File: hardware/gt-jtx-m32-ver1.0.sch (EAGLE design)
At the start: 11 parts, among them IC1 MEGA32-P

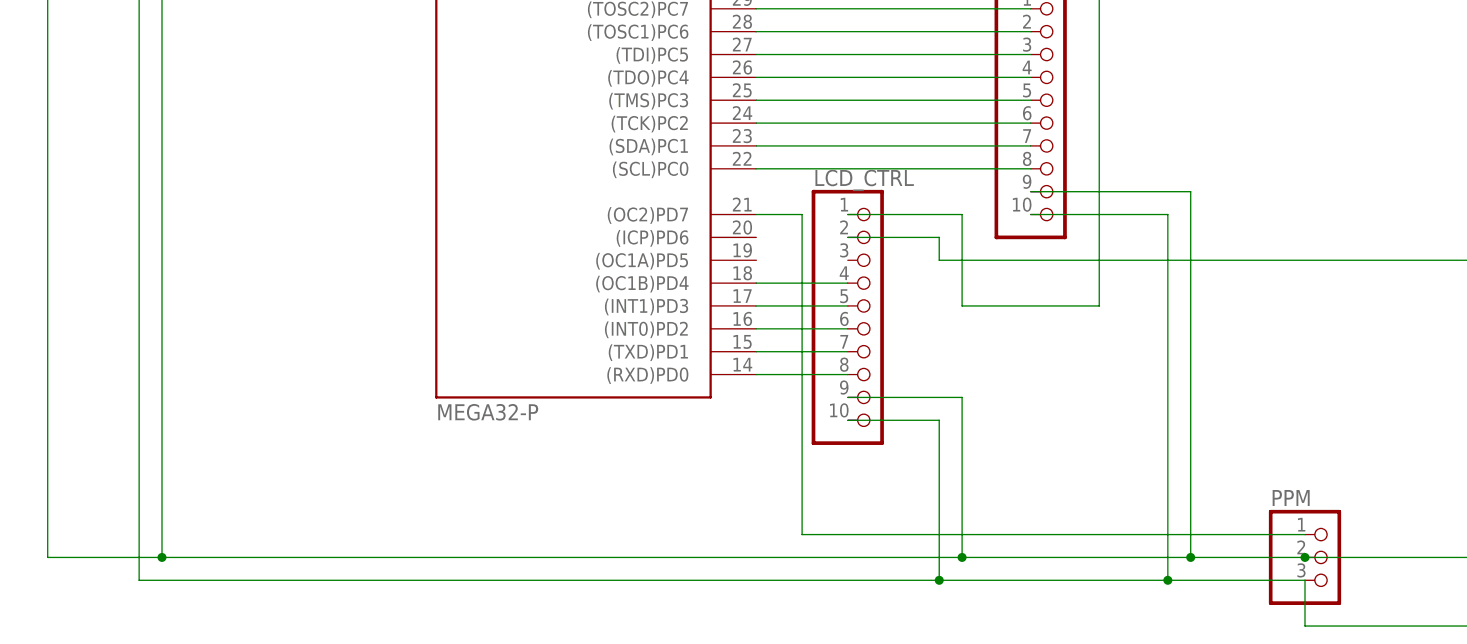
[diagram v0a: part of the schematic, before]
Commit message: added speaker and switch ports changed ppm pin to PD5
git-svn-id: https://gt-jtx.googlecode.com/svn/trunk@69 79910f2a-facc-22ab-b1ea-80da55196309
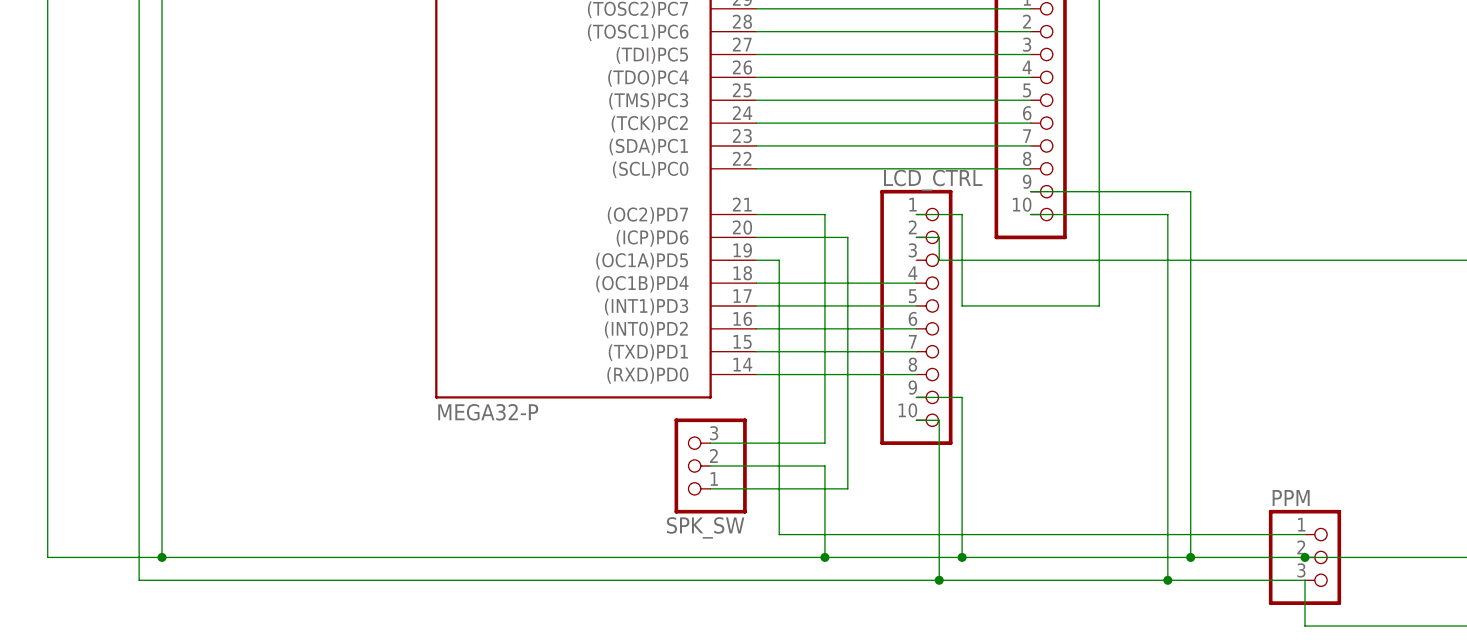
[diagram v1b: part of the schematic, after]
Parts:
- added SPK_SW: (no value), pinhead:PINHD-1X3
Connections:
- removed net GND: ANALOG.1, IC1.GND, IC1.GND@1, LCD_CTRL.9, LCD_DATA.9, LED.C, PPM.2, PWR.2, TRIMS.1, VR1.E
- new net N$5: IC1.(ICP)PD6, SPK_SW.1
- new net N$6: IC1.(OC2)PD7, SPK_SW.3
- new net SPK_SW: ANALOG.1, IC1.GND, IC1.GND@1, LCD_CTRL.9, LCD_DATA.9, LED.C, PPM.2, PWR.2, SPK_SW.2, TRIMS.1, VR1.E
- net N$15: now also IC1.(OC1A)PD5; no longer IC1.(OC2)PD7
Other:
- moved on the sheet: LCD_CTRL
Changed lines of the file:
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@@
 <part name="LCD_CTRL" library="pinhead" deviceset="PINHD-1X10" device=""/>
 <part name="LCD_DATA" library="pinhead" deviceset="PINHD-1X10" device=""/>
+<part name="SPK_SW" library="pinhead" deviceset="PINHD-1X3" device=""/>
 </parts>
 <sheets>
@@
 <instance part="ISP" gate="A" x="162.56" y="144.78"/>
 <instance part="IC1" gate="G$1" x="93.98" y="124.46"/>
-<instance part="LCD_CTRL" gate="A" x="127" y="88.9"/>
+<instance part="LCD_CTRL" gate="A" x="134.62" y="88.9"/>
 <instance part="LCD_DATA" gate="A" x="147.32" y="111.76"/>
+<instance part="SPK_SW" gate="A" x="106.68" y="71.12" rot="R180"/>
 </instances>
 <busses>
@@
 <pinref part="LCD_CTRL" gate="A" pin="10"/>
 <wire x1="205.74" y1="106.68" x2="205.74" y2="142.24" width="0.1524" layer="91"/>
-<wire x1="124.46" y1="76.2" x2="134.62" y2="76.2" width="0.1524" layer="91"/>
+<wire x1="132.08" y1="76.2" x2="134.62" y2="76.2" width="0.1524" layer="91"/>
 <wire x1="134.62" y1="76.2" x2="134.62" y2="58.42" width="0.1524" layer="91"/>
 <junction x="134.62" y="58.42"/>
@@
 </segment>
 </net>
-<net name="GND" class="0">
+<net name="SPK_SW" class="0">
 <segment>
 <wire x1="73.66" y1="144.78" x2="48.26" y2="144.78" width="0.1524" layer="91"/>
@@
 <wire x1="35.56" y1="154.94" x2="35.56" y2="60.96" width="0.1524" layer="91"/>
 <wire x1="35.56" y1="60.96" x2="48.26" y2="60.96" width="0.1524" layer="91"/>
-<wire x1="48.26" y1="60.96" x2="137.16" y2="60.96" width="0.1524" layer="91"/>
+<wire x1="48.26" y1="60.96" x2="121.92" y2="60.96" width="0.1524" layer="91"/>
+<wire x1="121.92" y1="60.96" x2="137.16" y2="60.96" width="0.1524" layer="91"/>
 <wire x1="137.16" y1="60.96" x2="162.56" y2="60.96" width="0.1524" layer="91"/>
 <wire x1="162.56" y1="60.96" x2="175.26" y2="60.96" width="0.1524" layer="91"/>
@@
 <pinref part="LCD_CTRL" gate="A" pin="9"/>
 <wire x1="220.98" y1="106.68" x2="220.98" y2="147.32" width="0.1524" layer="91"/>
-<wire x1="124.46" y1="78.74" x2="137.16" y2="78.74" width="0.1524" layer="91"/>
+<wire x1="132.08" y1="78.74" x2="137.16" y2="78.74" width="0.1524" layer="91"/>
 <wire x1="137.16" y1="78.74" x2="137.16" y2="60.96" width="0.1524" layer="91"/>
 <junction x="137.16" y="60.96"/>
@@
 <wire x1="162.56" y1="101.6" x2="162.56" y2="60.96" width="0.1524" layer="91"/>
 <junction x="162.56" y="60.96"/>
+<pinref part="SPK_SW" gate="A" pin="2"/>
+<wire x1="109.22" y1="71.12" x2="121.92" y2="71.12" width="0.1524" layer="91"/>
+<wire x1="121.92" y1="71.12" x2="121.92" y2="60.96" width="0.1524" layer="91"/>
+<junction x="121.92" y="60.96"/>
 </segment>
 </net>
@@
 <junction x="73.66" y="167.64"/>
 <pinref part="LCD_CTRL" gate="A" pin="1"/>
-<wire x1="124.46" y1="99.06" x2="137.16" y2="99.06" width="0.1524" layer="91"/>
+<wire x1="132.08" y1="99.06" x2="137.16" y2="99.06" width="0.1524" layer="91"/>
 <wire x1="137.16" y1="99.06" x2="137.16" y2="88.9" width="0.1524" layer="91"/>
 <wire x1="137.16" y1="88.9" x2="152.4" y2="88.9" width="0.1524" layer="91"/>
@@
 <pinref part="IC1" gate="G$1" pin="(RXD)PD0"/>
 <pinref part="LCD_CTRL" gate="A" pin="8"/>
-<wire x1="114.3" y1="81.28" x2="124.46" y2="81.28" width="0.1524" layer="91"/>
+<wire x1="114.3" y1="81.28" x2="132.08" y2="81.28" width="0.1524" layer="91"/>
 </segment>
 </net>
@@
 <pinref part="IC1" gate="G$1" pin="(TXD)PD1"/>
 <pinref part="LCD_CTRL" gate="A" pin="7"/>
-<wire x1="114.3" y1="83.82" x2="124.46" y2="83.82" width="0.1524" layer="91"/>
+<wire x1="114.3" y1="83.82" x2="132.08" y2="83.82" width="0.1524" layer="91"/>
 </segment>
 </net>
@@
 <pinref part="IC1" gate="G$1" pin="(INT0)PD2"/>
 <pinref part="LCD_CTRL" gate="A" pin="6"/>
-<wire x1="114.3" y1="86.36" x2="124.46" y2="86.36" width="0.1524" layer="91"/>
+<wire x1="114.3" y1="86.36" x2="132.08" y2="86.36" width="0.1524" layer="91"/>
 </segment>
 </net>
@@
 <pinref part="IC1" gate="G$1" pin="(INT1)PD3"/>
 <pinref part="LCD_CTRL" gate="A" pin="5"/>
-<wire x1="114.3" y1="88.9" x2="124.46" y2="88.9" width="0.1524" layer="91"/>
+<wire x1="114.3" y1="88.9" x2="132.08" y2="88.9" width="0.1524" layer="91"/>
 </segment>
 </net>
@@
 <pinref part="IC1" gate="G$1" pin="(OC1B)PD4"/>
 <pinref part="LCD_CTRL" gate="A" pin="4"/>
-<wire x1="114.3" y1="91.44" x2="124.46" y2="91.44" width="0.1524" layer="91"/>
+<wire x1="114.3" y1="91.44" x2="132.08" y2="91.44" width="0.1524" layer="91"/>
 </segment>
 </net>
@@
 <segment>
 <pinref part="LCD_CTRL" gate="A" pin="2"/>
-<wire x1="124.46" y1="96.52" x2="134.62" y2="96.52" width="0.1524" layer="91"/>
+<wire x1="132.08" y1="96.52" x2="134.62" y2="96.52" width="0.1524" layer="91"/>
 <wire x1="134.62" y1="96.52" x2="134.62" y2="93.98" width="0.1524" layer="91"/>
 <wire x1="134.62" y1="93.98" x2="213.36" y2="93.98" width="0.1524" layer="91"/>
@@
 <net name="N$15" class="0">
 <segment>
+<pinref part="PPM" gate="A" pin="1"/>
+<wire x1="116.84" y1="93.98" x2="116.84" y2="63.5" width="0.1524" layer="91"/>
+<wire x1="116.84" y1="63.5" x2="175.26" y2="63.5" width="0.1524" layer="91"/>
+<pinref part="IC1" gate="G$1" pin="(OC1A)PD5"/>
+<wire x1="114.3" y1="93.98" x2="116.84" y2="93.98" width="0.1524" layer="91"/>
+</segment>
+</net>
+<net name="N$5" class="0">
+<segment>
+<pinref part="SPK_SW" gate="A" pin="1"/>
+<wire x1="109.22" y1="68.58" x2="124.46" y2="68.58" width="0.1524" layer="91"/>
+<wire x1="124.46" y1="68.58" x2="124.46" y2="96.52" width="0.1524" layer="91"/>
+<pinref part="IC1" gate="G$1" pin="(ICP)PD6"/>
+<wire x1="124.46" y1="96.52" x2="114.3" y2="96.52" width="0.1524" layer="91"/>
+</segment>
+</net>
+<net name="N$6" class="0">
+<segment>
+<pinref part="SPK_SW" gate="A" pin="3"/>
+<wire x1="109.22" y1="73.66" x2="121.92" y2="73.66" width="0.1524" layer="91"/>
+<wire x1="121.92" y1="73.66" x2="121.92" y2="99.06" width="0.1524" layer="91"/>
 <pinref part="IC1" gate="G$1" pin="(OC2)PD7"/>
-<wire x1="114.3" y1="99.06" x2="119.38" y2="99.06" width="0.1524" layer="91"/>
-<wire x1="119.38" y1="99.06" x2="119.38" y2="63.5" width="0.1524" layer="91"/>
-<pinref part="PPM" gate="A" pin="1"/>
-<wire x1="119.38" y1="63.5" x2="175.26" y2="63.5" width="0.1524" layer="91"/>
-</segment>
-</net>
+<wire x1="121.92" y1="99.06" x2="114.3" y2="99.06" width="0.1524" layer="91"/>
+</segment>
+</net>

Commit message: fixed some of the hardware design
git-svn-id: https://gt-jtx.googlecode.com/svn/trunk@70 79910f2a-facc-22ab-b1ea-80da55196309
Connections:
- removed net N$33: IC1.(MOSI)PB5, ISP.6, TRIMS.5
- removed net N$34: IC1.(MISO)PB6, ISP.5, TRIMS.4
- removed net RST: IC1.RESET, ISP.1, LCD_CTRL.1, R2.2
- removed net SPK_SW: ANALOG.1, IC1.GND, IC1.GND@1, LCD_CTRL.9, LCD_DATA.9, LED.C, PPM.2, PWR.2, SPK_SW.2, TRIMS.1, VR1.E
- new net GND: ANALOG.1, IC1.GND, IC1.GND@1, ISP.1, LCD_CTRL.2, LCD_DATA.9, LED.C, PPM.2, PWR.2, SPK_SW.2, TRIMS.2, VR1.E
- new net N$12: IC1.(MOSI)PB5, ISP.6
- new net N$13: IC1.(MISO)PB6, ISP.2
- new net N$14: IC1.(SCK)PB7, ISP.3
- new net N$9: IC1.RESET, ISP.4, LCD_CTRL.10, R2.2
- net +5V: now also ISP.5, LCD_CTRL.1, TRIMS.1; no longer ISP.3, LCD_CTRL.10, TRIMS.2
- net CONTRA_ADJ: now also LCD_CTRL.3; no longer LCD_CTRL.2
- net N$28: no longer IC1.(SCK)PB7, ISP.4
